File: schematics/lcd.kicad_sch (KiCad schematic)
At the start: 5 parts, among them U22 ATF22V10C-7, U23 74HC245, U24 74HC373

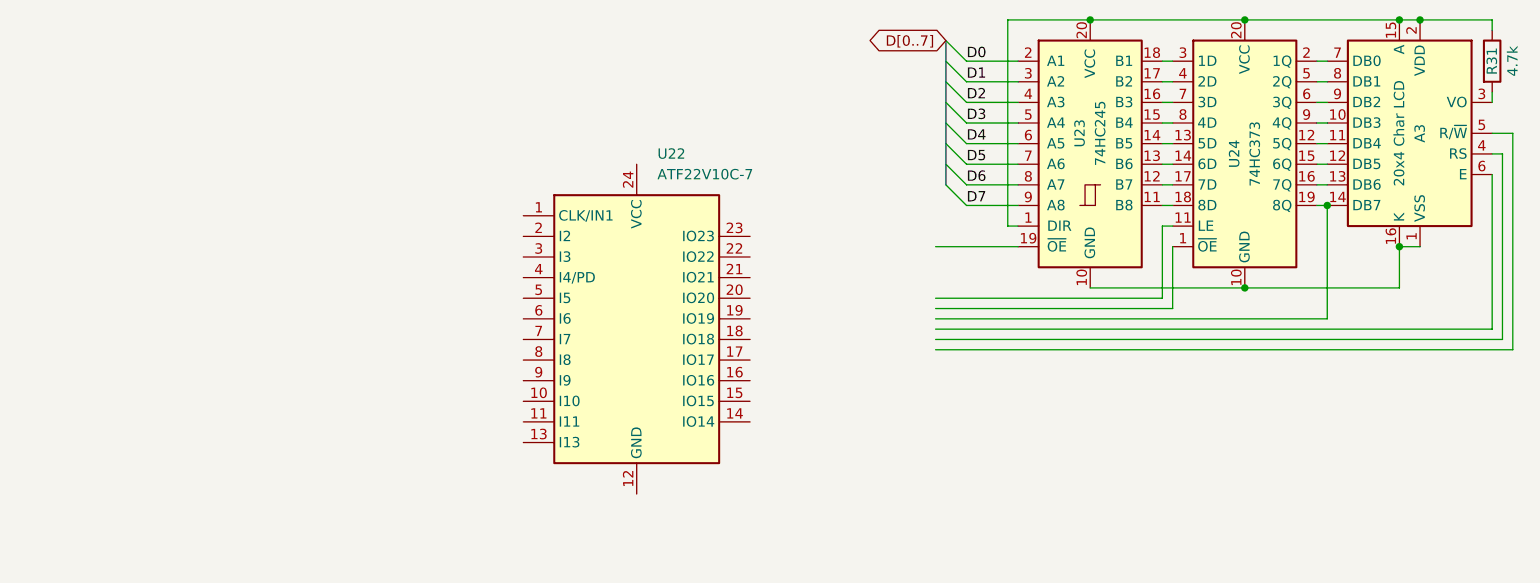
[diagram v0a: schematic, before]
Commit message: PLD files and schematics for address decoder, device selector, keyboard controller, lcd controller, banked memory, and bootloader.
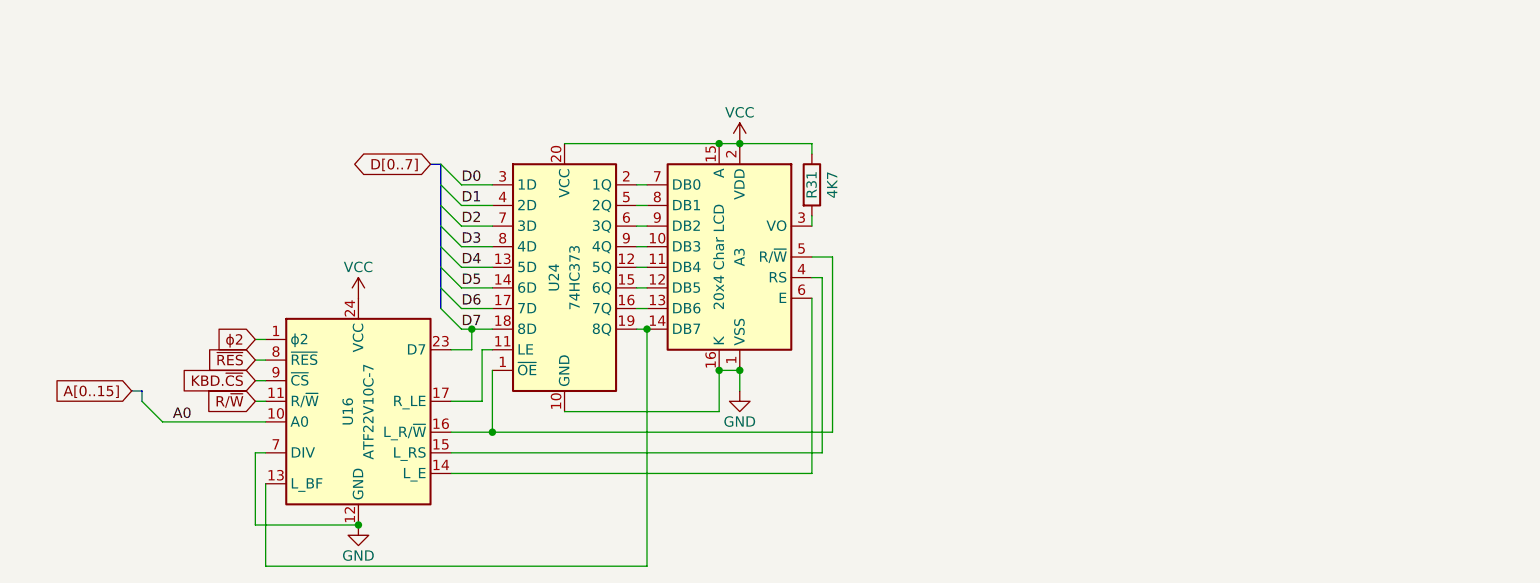
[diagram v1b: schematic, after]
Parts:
- removed U22: ATF22V10C-7, Package_DIP:DIP-24_W7.62mm, symbol Logic_Programmable:PEEL22CV10AP
- removed U23: 74HC245, symbol 74xx:74HC245
- added U16: ATF22V10C-7, Package_DIP:DIP-24_W7.62mm, symbol Logic_Programmable:PEEL22CV10AP
- R31: value 4.7k -> 4K7
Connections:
- net D0: now also U24.3 (1D)
- net D1: now also U24.4 (2D)
- net D2: now also U24.7 (3D)
- net D3: now also U24.8 (4D)
- net D4: now also U24.13 (5D)
- net D5: now also U24.14 (6D)
- net D6: now also U24.17 (7D)
- net D7: now also U24.18 (8D), U16.23 (D7)
- net VCC: now reaches A3.15 (A), A3.2 (VDD), R31.1, U24.20 (VCC)
- net VCC: now also U16.24 (VCC)
- net GND: now reaches A3.1 (VSS), A3.16 (K), U24.10 (GND)
- net GND: now also U16.12 (GND), U16.7 (DIV)
- net at A3.14 (DB7), U24.19 (8Q): now also U16.13 (L_BF)
- net at A3.4 (RS): now also U16.15 (L_RS)
- net at A3.5 (R/~{W}): now also U24.1 (~{OE}), U16.16 (L_R/~{W})
- net at A3.6 (E): now also U16.14 (L_E)
- net at U24.11 (LE): now also U16.17 (R_LE)
- new net A0: U16.10 (A0)
- new net KBD.~{CS}: U16.9 (~{CS})
- new net R/~{W}: U16.11 (R/~{W})
- new net ~{RES}: U16.8 (~{RES})
- new net ϕ2: U16.1 (ϕ2)
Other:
- moved on the sheet: A3, R31, U24

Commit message: added phi0 for write latch timing
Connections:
- net GND: no longer U16.7 (DIV)
- net ϕ2: now also U16.2 (ϕ2); no longer U16.1 (ϕ2)
- new net ϕ0: U16.1 (ϕ0)
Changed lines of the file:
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@@
-	)
-	(junction
-		(at 116.84 121.92)
-		(diameter 0)
-		(color 0 0 0 0)
 	)
 	(junction
@@
 	)
 	(bus_entry
-		(at 90.17 106.68)
+		(at 88.9 106.68)
 		(size 2.54 2.54)
 		(stroke
@@
 	(bus
 		(pts
-			(xy 90.17 105.41) (xy 90.17 106.68)
+			(xy 88.9 105.41) (xy 88.9 106.68)
 		)
 		(stroke
@@
 	(wire
 		(pts
-			(xy 92.71 109.22) (xy 105.41 109.22)
+			(xy 91.44 109.22) (xy 105.41 109.22)
 		)
 		(stroke
@@
 	(wire
 		(pts
-			(xy 104.14 121.92) (xy 116.84 121.92)
-		)
-		(stroke
-			(width 0)
-			(type default)
-		)
-	)
-	(wire
-		(pts
 			(xy 172.72 74.93) (xy 163.83 74.93)
 		)
@@
 		)
 	)
+	(wire
+		(pts
+			(xy 104.14 101.6) (xy 105.41 101.6)
+		)
+		(stroke
+			(width 0)
+			(type default)
+		)
+	)
 	(bus
 		(pts
@@
 		)
 	)
-	(wire
-		(pts
-			(xy 105.41 113.03) (xy 104.14 113.03)
-		)
-		(stroke
-			(width 0)
-			(type default)
-		)
-	)
 	(bus
 		(pts
@@
 	(wire
 		(pts
+			(xy 104.14 111.76) (xy 105.41 111.76)
+		)
+		(stroke
+			(width 0)
+			(type default)
+		)
+	)
+	(wire
+		(pts
 			(xy 129.54 97.79) (xy 130.81 97.79)
 		)
@@
 	(wire
 		(pts
+			(xy 104.14 104.14) (xy 105.41 104.14)
+		)
+		(stroke
+			(width 0)
+			(type default)
+		)
+	)
+	(wire
+		(pts
 			(xy 161.29 107.95) (xy 161.29 102.87)
 		)
@@
 	(bus
 		(pts
-			(xy 88.9 105.41) (xy 90.17 105.41)
+			(xy 87.63 105.41) (xy 88.9 105.41)
 		)
 		(stroke
@@
 	(wire
 		(pts
+			(xy 104.14 106.68) (xy 105.41 106.68)
+		)
+		(stroke
+			(width 0)
+			(type default)
+		)
+	)
+	(wire
+		(pts
 			(xy 172.72 93.98) (xy 172.72 115.57)
 		)
@@
 	(wire
 		(pts
-			(xy 104.14 106.68) (xy 105.41 106.68)
-		)
-		(stroke
-			(width 0)
-			(type default)
-		)
-	)
-	(wire
-		(pts
 			(xy 161.29 102.87) (xy 163.83 102.87)
 		)
@@
 	(wire
 		(pts
-			(xy 104.14 101.6) (xy 105.41 101.6)
-		)
-		(stroke
-			(width 0)
-			(type default)
-		)
-	)
-	(wire
-		(pts
 			(xy 129.54 90.17) (xy 133.35 90.17)
 		)
@@
 	(wire
 		(pts
-			(xy 104.14 104.14) (xy 105.41 104.14)
-		)
-		(stroke
-			(width 0)
-			(type default)
-		)
-	)
-	(wire
-		(pts
 			(xy 129.54 87.63) (xy 133.35 87.63)
 		)
@@
 		(pts
 			(xy 129.54 92.71) (xy 133.35 92.71)
-		)
-		(stroke
-			(width 0)
-			(type default)
-		)
-	)
-	(wire
-		(pts
-			(xy 104.14 113.03) (xy 104.14 121.92)
 		)
 		(stroke
@@
 	)
 	(label "A0"
-		(at 93.98 109.22 0)
+		(at 91.44 109.22 0)
 		(effects
 			(font
@@
 	(global_label "R{slash}~{W}"
 		(shape input)
-		(at 104.14 106.68 180)
+		(at 104.14 111.76 180)
 		(fields_autoplaced yes)
 		(effects
@@
 		)
 		(property "Intersheetrefs" "${INTERSHEET_REFS}"
-			(at 97.1029 106.68 0)
+			(at 97.1029 111.76 0)
 			(hide yes)
 			(show_name no)
@@
 	(global_label "A[0..15]"
 		(shape input)
-		(at 88.9 105.41 180)
+		(at 87.63 105.41 180)
 		(fields_autoplaced yes)
 		(effects
@@
 		)
 		(property "Intersheetrefs" "${INTERSHEET_REFS}"
-			(at 78.2947 105.41 0)
+			(at 77.0247 105.41 0)
 			(hide yes)
 			(show_name no)
@@
 		)
 	)
-	(global_label "ϕ2"
+	(global_label "ϕ0"
 		(shape input)
 		(at 104.14 99.06 180)
@@
 		)
 	)
-	(global_label "KBD.~{CS}"
+	(global_label "ϕ2"
 		(shape input)
-		(at 104.14 104.14 180)
+		(at 104.14 101.6 180)
 		(fields_autoplaced yes)
 		(effects
@@
 		)
 		(property "Intersheetrefs" "${INTERSHEET_REFS}"
-			(at 94.2605 104.14 0)
+			(at 98.6148 101.6 0)
 			(hide yes)
 			(show_name no)
@@
 		)
 	)
+	(global_label "KBD.~{CS}"
+		(shape input)
+		(at 104.14 106.68 180)
+		(fields_autoplaced yes)
+		(effects
+			(font
+				(size 1.27 1.27)
+			)
+			(justify right)
+		)
+		(property "Intersheetrefs" "${INTERSHEET_REFS}"
+			(at 94.2605 106.68 0)
+			(hide yes)
+			(show_name no)
+			(do_not_autoplace no)
+			(effects
+				(font
+					(size 1.27 1.27)
+				)
+				(justify right)
+			)
+		)
+	)
 	(global_label "~{RES}"
 		(shape input)
-		(at 104.14 101.6 180)
+		(at 104.14 104.14 180)
 		(fields_autoplaced yes)
 		(effects
@@
 		)
 		(property "Intersheetrefs" "${INTERSHEET_REFS}"
-			(at 97.5263 101.6 0)
+			(at 97.5263 104.14 0)
 			(hide yes)
 			(show_name no)

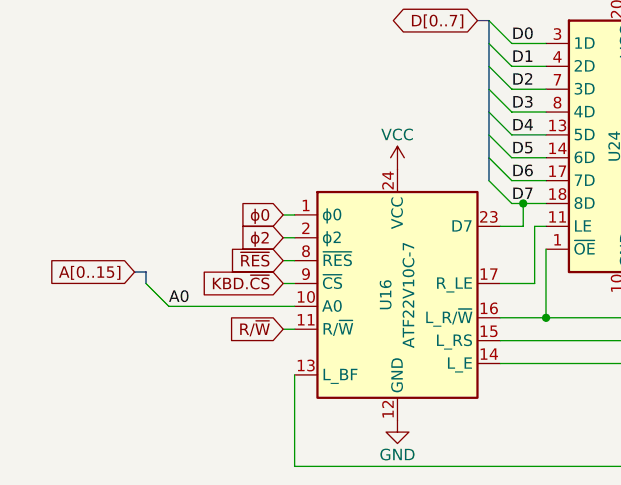
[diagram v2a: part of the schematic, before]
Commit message: fixes to bootloader; finished via schematic
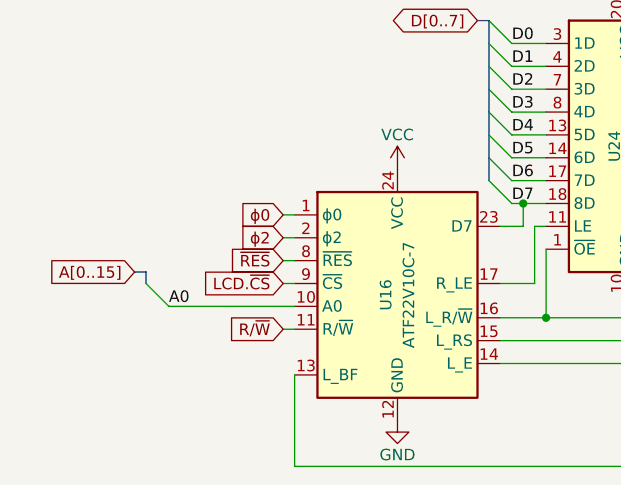
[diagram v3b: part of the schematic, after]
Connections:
- net KBD.~{CS} renamed LCD.~{CS}
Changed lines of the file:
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@@
 		)
 	)
-	(global_label "KBD.~{CS}"
+	(global_label "LCD.~{CS}"
 		(shape input)
 		(at 104.14 106.68 180)
@@
 		)
 		(property "Intersheetrefs" "${INTERSHEET_REFS}"
-			(at 94.2605 106.68 0)
+			(at 94.5024 106.68 0)
 			(hide yes)
 			(show_name no)

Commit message: updating schematics as I wire the board
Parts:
- renumbered A3 to A2, R31 to R43, U16 to U27, U24 to U28
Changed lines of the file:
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@@
 		(in_pos_files yes)
 		(dnp no)
-		(property "Reference" "#PWR055"
+		(property "Reference" "#PWR067"
 			(at 116.84 128.27 0)
 			(hide yes)
@@
 			(project "bv6502_hw"
 				(path "/94c72abe-aaa5-49aa-8ab7-5d3e7cbc10be/ce02b87a-0b7e-446c-8a51-e177c4556bd7"
-					(reference "#PWR055")
+					(reference "#PWR067")
 					(unit 1)
 				)
@@
 		(in_pos_files yes)
 		(dnp no)
-		(property "Reference" "U16"
+		(property "Reference" "U27"
 			(at 115.57 107.95 90)
 			(show_name no)
@@
 			(project "bv6502_hw"
 				(path "/94c72abe-aaa5-49aa-8ab7-5d3e7cbc10be/ce02b87a-0b7e-446c-8a51-e177c4556bd7"
-					(reference "U16")
+					(reference "U27")
 					(unit 1)
 				)
@@
 		(in_pos_files yes)
 		(dnp no)
-		(property "Reference" "R31"
+		(property "Reference" "R43"
 			(at 172.72 80.01 90)
 			(show_name no)
@@
 			(project "bv6502_hw"
 				(path "/94c72abe-aaa5-49aa-8ab7-5d3e7cbc10be/ce02b87a-0b7e-446c-8a51-e177c4556bd7"
-					(reference "R31")
+					(reference "R43")
 					(unit 1)
 				)
@@
 		(in_pos_files yes)
 		(dnp no)
-		(property "Reference" "A3"
+		(property "Reference" "A2"
 			(at 163.83 88.9 90)
 			(show_name no)
@@
 			(project "bv6502_hw"
 				(path "/94c72abe-aaa5-49aa-8ab7-5d3e7cbc10be/ce02b87a-0b7e-446c-8a51-e177c4556bd7"
-					(reference "A3")
+					(reference "A2")
 					(unit 1)
 				)
@@
 		(dnp no)
 		(fields_autoplaced yes)
-		(property "Reference" "U24"
+		(property "Reference" "U28"
 			(at 140.97 91.44 90)
 			(show_name no)
@@
 			(project "bv6502_hw"
 				(path "/94c72abe-aaa5-49aa-8ab7-5d3e7cbc10be/ce02b87a-0b7e-446c-8a51-e177c4556bd7"
-					(reference "U24")
+					(reference "U28")
 					(unit 1)
 				)
@@
 		(in_pos_files yes)
 		(dnp no)
-		(property "Reference" "#PWR040"
+		(property "Reference" "#PWR069"
 			(at 163.83 111.76 0)
 			(hide yes)
@@
 			(project "bv6502_hw"
 				(path "/94c72abe-aaa5-49aa-8ab7-5d3e7cbc10be/ce02b87a-0b7e-446c-8a51-e177c4556bd7"
-					(reference "#PWR040")
+					(reference "#PWR069")
 					(unit 1)
 				)
@@
 		(in_pos_files yes)
 		(dnp no)
-		(property "Reference" "#PWR034"
+		(property "Reference" "#PWR068"
 			(at 163.83 78.74 0)
 			(hide yes)
@@
 			(project "bv6502_hw"
 				(path "/94c72abe-aaa5-49aa-8ab7-5d3e7cbc10be/ce02b87a-0b7e-446c-8a51-e177c4556bd7"
-					(reference "#PWR034")
+					(reference "#PWR068")
 					(unit 1)
 				)
@@
 		(in_pos_files yes)
 		(dnp no)
-		(property "Reference" "#PWR054"
+		(property "Reference" "#PWR066"
 			(at 116.84 97.79 0)
 			(hide yes)
@@
 			(project "bv6502_hw"
 				(path "/94c72abe-aaa5-49aa-8ab7-5d3e7cbc10be/ce02b87a-0b7e-446c-8a51-e177c4556bd7"
-					(reference "#PWR054")
+					(reference "#PWR066")
 					(unit 1)
 				)

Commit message: fixing wiring
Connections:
- net D7: now also U27.18 (D7); no longer U27.23 (D7)

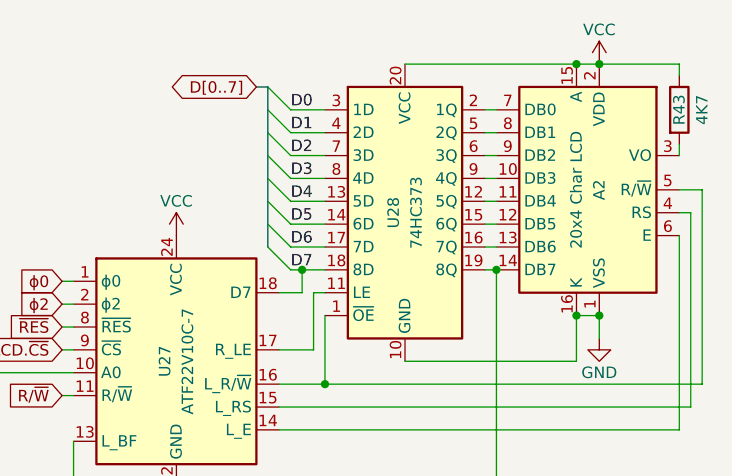
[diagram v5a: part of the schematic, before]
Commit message: my keyboard needed a transceiver after all :(
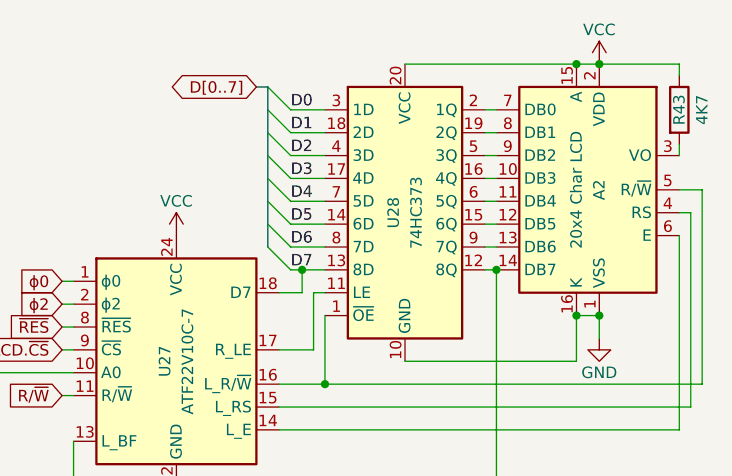
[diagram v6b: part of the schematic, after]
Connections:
- net D1: now also U28.18 (2D); no longer U28.4 (2D)
- net D2: now also U28.4 (3D); no longer U28.7 (3D)
- net D3: now also U28.17 (4D); no longer U28.8 (4D)
- net D4: now also U28.7 (5D); no longer U28.13 (5D)
- net D6: now also U28.8 (7D); no longer U28.17 (7D)
- net D7: now also U28.13 (8D); no longer U28.18 (8D)
- net at A2.14 (DB7), U27.13 (L_BF): now also U28.12 (8Q); no longer U28.19 (8Q)
- net at A2.10 (DB3): now also U28.16 (4Q); no longer U28.9 (4Q)
- net at A2.11 (DB4): now also U28.6 (5Q); no longer U28.12 (5Q)
- net at A2.13 (DB6): now also U28.9 (7Q); no longer U28.16 (7Q)
- net at A2.8 (DB1): now also U28.19 (2Q); no longer U28.5 (2Q)
- net at A2.9 (DB2): now also U28.5 (3Q); no longer U28.6 (3Q)

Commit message: clock improvements
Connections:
- net ϕ0 renamed ϕ0.0
- net ϕ2 renamed ϕ2.0
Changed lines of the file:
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@@
 		)
 	)
-	(global_label "ϕ0"
+	(global_label "ϕ0.0"
 		(shape input)
 		(at 104.14 99.06 180)
@@
 		)
 		(property "Intersheetrefs" "${INTERSHEET_REFS}"
-			(at 98.6148 99.06 0)
+			(at 96.8005 99.06 0)
 			(hide yes)
 			(show_name no)
@@
 		)
 	)
-	(global_label "ϕ2"
+	(global_label "ϕ2.0"
 		(shape input)
 		(at 104.14 101.6 180)
@@
 		)
 		(property "Intersheetrefs" "${INTERSHEET_REFS}"
-			(at 98.6148 101.6 0)
+			(at 96.8005 101.6 0)
 			(hide yes)
 			(show_name no)

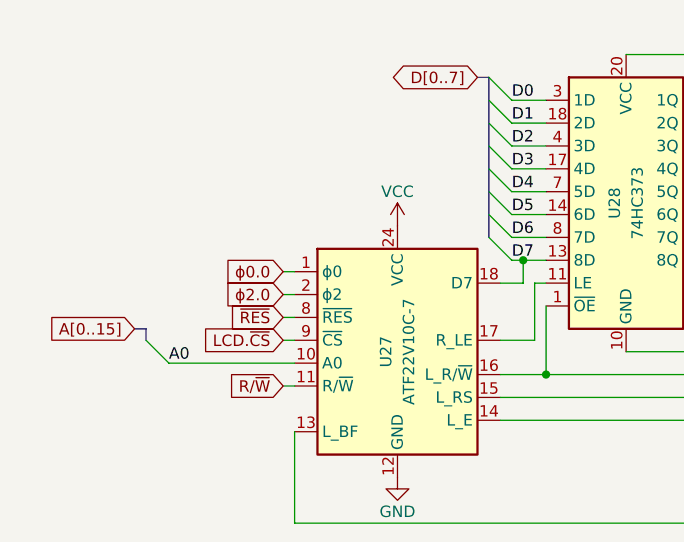
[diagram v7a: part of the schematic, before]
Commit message: ditched phi0, dropped to 6MHz
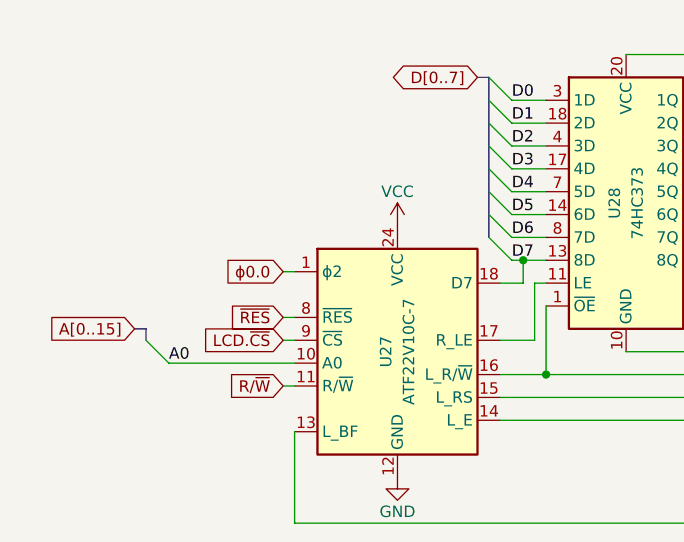
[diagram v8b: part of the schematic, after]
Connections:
- net ϕ2.0: no longer names the net of U27.2
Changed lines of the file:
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@@
-		)
-	)
-	(wire
-		(pts
-			(xy 104.14 101.6) (xy 105.41 101.6)
-		)
-		(stroke
-			(width 0)
-			(type default)
 		)
 	)
@@
 			(hide yes)
 			(show_name no)
-			(do_not_autoplace no)
-			(effects
-				(font
-					(size 1.27 1.27)
-				)
-				(justify right)
-			)
-		)
-	)
-	(global_label "ϕ2.0"
-		(shape input)
-		(at 104.14 101.6 180)
-		(fields_autoplaced yes)
-		(effects
-			(font
-				(size 1.27 1.27)
-			)
-			(justify right)
-		)
-		(property "Intersheetrefs" "${INTERSHEET_REFS}"
-			(at 96.8005 101.6 0)
-			(hide yes)
-			(show_name no)
